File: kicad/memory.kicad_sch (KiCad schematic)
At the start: 4 parts, among them J1 MEM2051-00-195-00-A_REVC, U9 GD25Q40CEIGR

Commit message: Connected all remaining unconnected pins
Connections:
- net GPIO_CD: now reaches J1.9 (CD)
- net QSPI_SS: now reaches U9.1 (CS#)
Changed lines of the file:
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@@
+    )
+  )
+  (global_label "QSPI_SS" (shape input) (at 86.36 81.28 180) (fields_autoplaced)
+    (effects (font (size 1.27 1.27)) (justify right))
+    (property "Intersheet References" "${INTERSHEET_REFS}" (id 0) (at 76.1455 81.2006 0)
+      (effects (font (size 1.27 1.27)) (justify right) hide)
     )
   )
@@
       (effects (font (size 1.27 1.27)) (justify right) hide)
     )
+  )
+  (global_label "GPIO_CD" (shape output) (at 180.34 100.33 180) (fields_autoplaced)
+    (effects (font (size 1.27 1.27)) (justify right))
+    (property "Intersheet References" "${INTERSHEET_REFS}" (id 0) (at 169.944 100.2506 0)
+      (effects (font (size 1.27 1.27)) (justify right) hide)
+    )

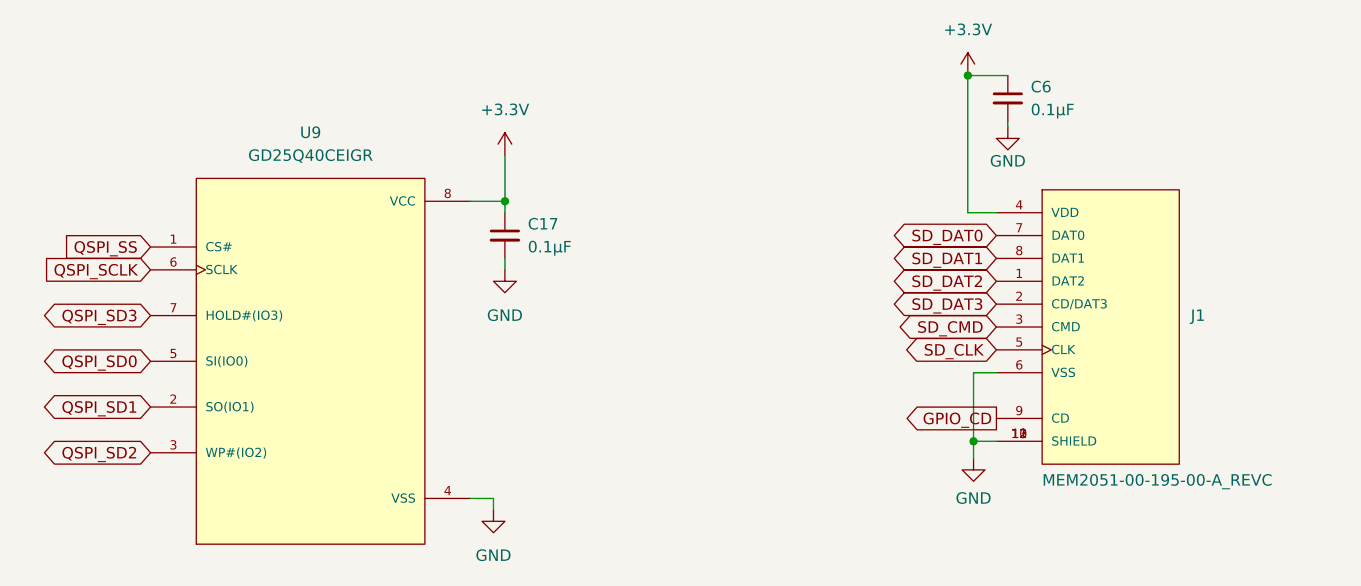
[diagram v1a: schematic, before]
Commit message: Updated schematic with various changes
Increased size of small components
Updated title/spec sheet
Cleaned footprints
Other small changes as well
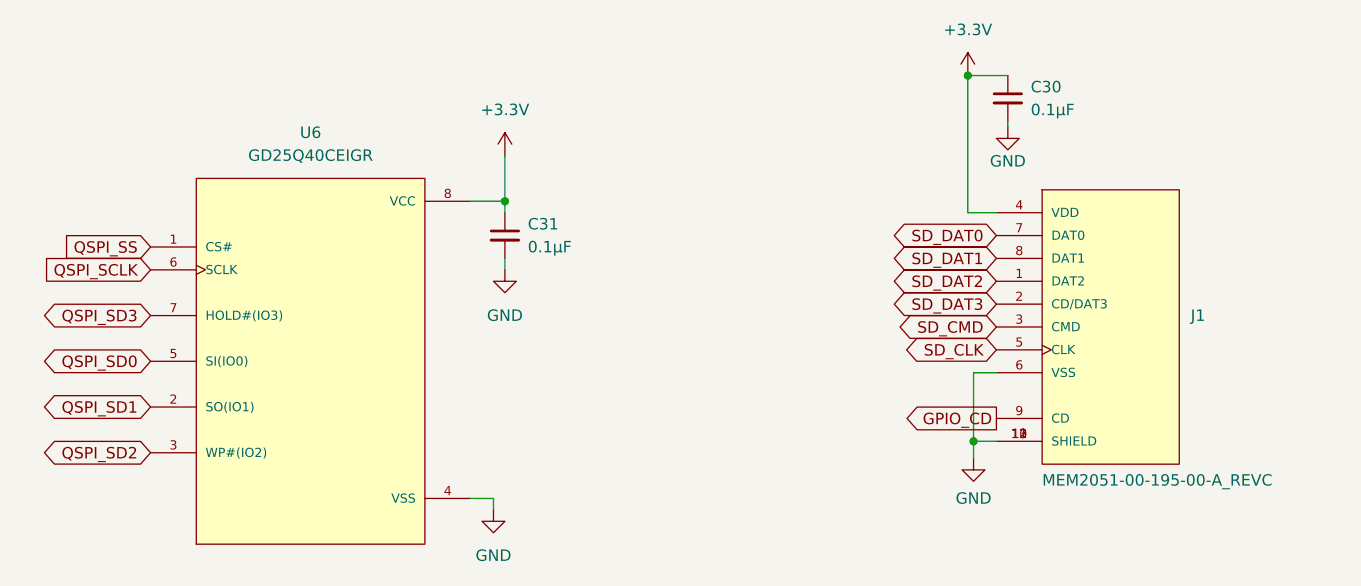
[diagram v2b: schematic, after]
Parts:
- C30: renamed from C6; footprint personal:C_0201_0603Metric -> personal:C_0402_1005Metric
- C31: renamed from C17; footprint personal:C_0201_0603Metric -> personal:C_0402_1005Metric
- renumbered U9 to U6
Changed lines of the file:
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@@
   (symbol (lib_id "power:+3.3V") (at 125.73 71.12 0) (unit 1)
     (in_bom yes) (on_board yes) (fields_autoplaced)
-    (property "Reference" "#PWR0107" (id 0) (at 125.73 74.93 0)
+    (property "Reference" "#PWR036" (id 0) (at 125.73 74.93 0)
       (effects (font (size 1.27 1.27)) hide)
     )
@@
   (symbol (lib_id "personal:GD25Q40CEIGR") (at 104.14 93.98 0) (unit 1)
     (in_bom yes) (on_board yes) (fields_autoplaced)
-    (property "Reference" "U9" (id 0) (at 104.14 68.58 0))
+    (property "Reference" "U6" (id 0) (at 104.14 68.58 0))
     (property "Value" "GD25Q40CEIGR" (id 1) (at 104.14 71.12 0))
     (property "Footprint" "personal:PSON50P200X300X50-9N" (id 2) (at 104.14 93.98 0)
@@
   (symbol (lib_id "power:GND") (at 124.46 110.49 0) (unit 1)
     (in_bom yes) (on_board yes) (fields_autoplaced)
-    (property "Reference" "#PWR0106" (id 0) (at 124.46 116.84 0)
+    (property "Reference" "#PWR039" (id 0) (at 124.46 116.84 0)
       (effects (font (size 1.27 1.27)) hide)
     )
@@
   (symbol (lib_id "Device:C_Small") (at 125.73 80.01 0) (unit 1)
     (in_bom yes) (on_board yes) (fields_autoplaced)
-    (property "Reference" "C17" (id 0) (at 128.27 78.7462 0)
+    (property "Reference" "C31" (id 0) (at 128.27 78.7462 0)
       (effects (font (size 1.27 1.27)) (justify left))
     )
@@
       (effects (font (size 1.27 1.27)) (justify left))
     )
-    (property "Footprint" "personal:C_0201_0603Metric" (id 2) (at 125.73 80.01 0)
+    (property "Footprint" "personal:C_0402_1005Metric" (id 2) (at 125.73 80.01 0)
       (effects (font (size 1.27 1.27)) hide)
     )
@@
   (symbol (lib_id "power:GND") (at 181.61 67.945 0) (unit 1)
     (in_bom yes) (on_board yes)
-    (property "Reference" "#PWR011" (id 0) (at 181.61 74.295 0)
+    (property "Reference" "#PWR035" (id 0) (at 181.61 74.295 0)
       (effects (font (size 1.27 1.27)) hide)
     )
@@
   (symbol (lib_id "power:GND") (at 125.73 83.82 0) (unit 1)
     (in_bom yes) (on_board yes) (fields_autoplaced)
-    (property "Reference" "#PWR0108" (id 0) (at 125.73 90.17 0)
+    (property "Reference" "#PWR037" (id 0) (at 125.73 90.17 0)
       (effects (font (size 1.27 1.27)) hide)
     )
@@
   (symbol (lib_id "power:+3.3V") (at 177.165 62.23 0) (unit 1)
     (in_bom yes) (on_board yes) (fields_autoplaced)
-    (property "Reference" "#PWR010" (id 0) (at 177.165 66.04 0)
+    (property "Reference" "#PWR034" (id 0) (at 177.165 66.04 0)
       (effects (font (size 1.27 1.27)) hide)
     )
@@
   (symbol (lib_id "Device:C_Small") (at 181.61 64.77 0) (unit 1)
     (in_bom yes) (on_board yes) (fields_autoplaced)
-    (property "Reference" "C6" (id 0) (at 184.15 63.5062 0)
+    (property "Reference" "C30" (id 0) (at 184.15 63.5062 0)
       (effects (font (size 1.27 1.27)) (justify left))
     )
@@
       (effects (font (size 1.27 1.27)) (justify left))
     )
-    (property "Footprint" "personal:C_0201_0603Metric" (id 2) (at 181.61 64.77 0)
+    (property "Footprint" "personal:C_0402_1005Metric" (id 2) (at 181.61 64.77 0)
       (effects (font (size 1.27 1.27)) hide)
     )
@@
   (symbol (lib_id "power:GND") (at 177.8 104.775 0) (unit 1)
     (in_bom yes) (on_board yes) (fields_autoplaced)
-    (property "Reference" "#PWR012" (id 0) (at 177.8 111.125 0)
+    (property "Reference" "#PWR038" (id 0) (at 177.8 111.125 0)
       (effects (font (size 1.27 1.27)) hide)
     )
